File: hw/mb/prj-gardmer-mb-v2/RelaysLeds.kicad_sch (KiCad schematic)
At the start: 52 parts, among them K1 AZ9371T-1A-5D, K2 AZ9371T-1A-5D, K3 AZ9371T-1A-5D, K4 AZ9371T-1A-5D, Q1 BC817, Q13 BC817, Q14 BC817, Q2 BC817, Q3 BC817, Q4 BC817, U4 74HC595, U5 74HC595, U6 ULN2803A

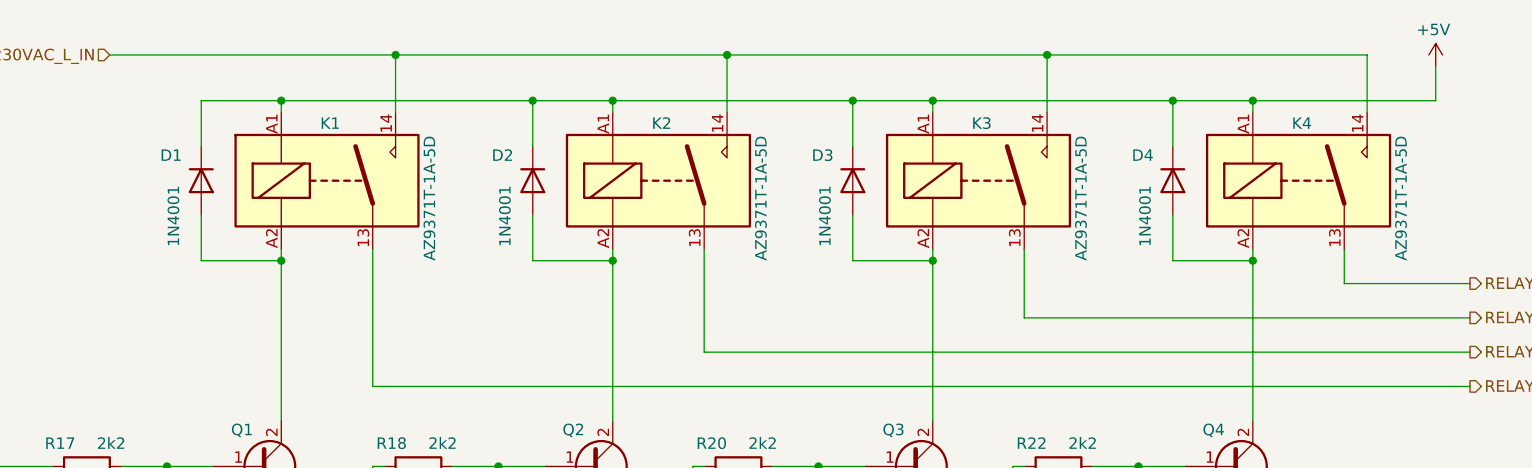
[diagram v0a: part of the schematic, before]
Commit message: Added footprints and bom. Updated schematics.
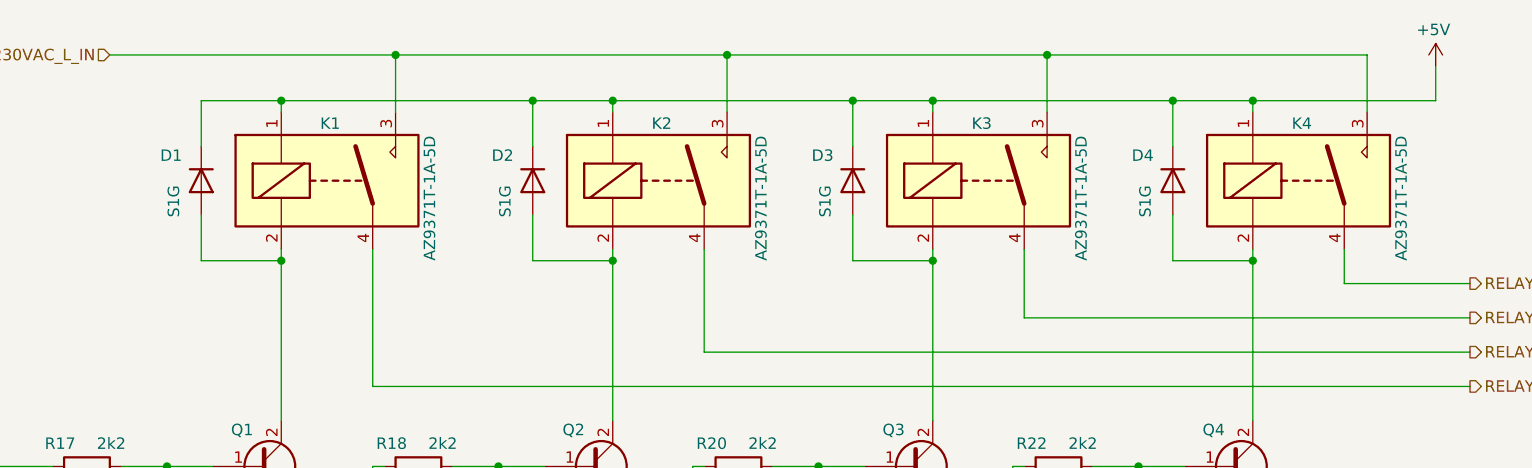
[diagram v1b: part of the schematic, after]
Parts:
- D1, D2, D3, D4: value 1N4001 -> S1G
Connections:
- net +5V: now also K1.1, K2.1, K3.1, K4.1; no longer K1.A1, K2.A1, K3.A1, K4.A1
- net 230VAC_L_IN: now also K1.3, K2.3, K3.3, K4.3; no longer K1.14, K2.14, K3.14, K4.14
- net RELAY1_OUT: now also K1.4; no longer K1.13
- net RELAY2_OUT: now also K2.4; no longer K2.13
- net RELAY3_OUT: now also K3.4; no longer K3.13
- net RELAY4_OUT: now also K4.4; no longer K4.13
- net at D4.2 (A), Q4.2 (C): now also K4.2; no longer K4.A2
- net at D1.2 (A), Q1.2 (C): now also K1.2; no longer K1.A2
- net at D2.2 (A), Q2.2 (C): now also K2.2; no longer K2.A2
- net at D3.2 (A), Q3.2 (C): now also K3.2; no longer K3.A2
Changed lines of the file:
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@@
 	)
 	(symbol
+		(lib_name "Relay_SPST-NO_1")
 		(lib_id "alf64:Relay_SPST-NO")
 		(at 138.43 31.75 0)
@@
 			)
 		)
-		(pin "13"
+		(pin "2"
 		)
-		(pin "A2"
+		(pin "1"
 		)
-		(pin "14"
+		(pin "3"
 		)
-		(pin "A1"
+		(pin "4"
 		)
 		(instances
@@
 			)
 		)
-		(property "Value" "1N4001"
+		(property "Value" "S1G"
 			(at 158.242 32.258 0)
 			(effects
@@
 			)
 		)
-		(property "Value" "1N4001"
+		(property "Value" "S1G"
 			(at 193.802 32.258 0)
 			(effects
@@
 	)
 	(symbol
+		(lib_name "Relay_SPST-NO_3")
 		(lib_id "alf64:Relay_SPST-NO")
 		(at 210.82 31.75 0)
@@
 			)
 		)
-		(pin "13"
+		(pin "1"
 		)
-		(pin "A2"
+		(pin "4"
 		)
-		(pin "14"
+		(pin "2"
 		)
-		(pin "A1"
+		(pin "3"
 		)
 		(instances
@@
 	)
 	(symbol
+		(lib_name "Relay_SPST-NO_2")
 		(lib_id "alf64:Relay_SPST-NO")
 		(at 175.26 31.75 0)
@@
 			)
 		)
-		(pin "13"
+		(pin "3"
 		)
-		(pin "A2"
+		(pin "1"
 		)
-		(pin "14"
+		(pin "2"
 		)
-		(pin "A1"
+		(pin "4"
 		)
 		(instances
@@
 			)
 		)
-		(property "Value" "1N4001"
+		(property "Value" "S1G"
 			(at 229.362 32.258 0)
 			(effects
@@
 			)
 		)
-		(pin "13"
+		(pin "1"
 		)
-		(pin "A2"
+		(pin "4"
 		)
-		(pin "14"
+		(pin "3"
 		)
-		(pin "A1"
+		(pin "2"
 		)
 		(instances
@@
 			)
 		)
-		(property "Value" "1N4001"
+		(property "Value" "S1G"
 			(at 121.412 32.258 0)
 			(effects

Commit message: Assigned footprints to schematic symbols.
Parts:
- C14, C15, C16, R16, R17, R18, R19, R20, R21, R22, R23, R24, R25, R26, R27, R28, R29, R30, R31, R48, R49, R50, R51, R52, R53: footprint (none) -> alf64:Generic_0805
- D1, D2, D3, D4: footprint (none) -> alf64:D_SMA
- D10, D11, D12, D13, D14, D5, D6, D7, D8, D9: footprint (none) -> alf64:D_0805
- K1, K2, K3, K4: footprint (none) -> alf64:relay_AZ9371
- Q1, Q13, Q14, Q2, Q3, Q4: footprint (none) -> alf64:SOT-23-3
- U4, U5: footprint (none) -> alf64:SO-16_3.9x9.9mm_P1.27mm
- U6: footprint (none) -> alf64:SOP-18_7x12.5mm_P1.27mm
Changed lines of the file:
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@@
 			)
 		)
-		(property "Footprint" ""
+		(property "Footprint" "alf64:SOT-23-3"
 			(at 243.84 60.96 0)
 			(effects
@@
 			)
 		)
-		(property "Footprint" ""
+		(property "Footprint" "alf64:Generic_0805"
 			(at 191.262 68.58 90)
 			(effects
@@
 			)
 		)
-		(property "Footprint" ""
+		(property "Footprint" "alf64:Generic_0805"
 			(at 53.0352 35.56 0)
 			(effects
@@
 			)
 		)
-		(property "Footprint" ""
+		(property "Footprint" "alf64:relay_AZ9371"
 			(at 149.86 33.02 0)
 			(effects
@@
 			)
 		)
-		(property "Footprint" ""
+		(property "Footprint" "alf64:D_SMA"
 			(at 161.29 31.75 0)
 			(effects
@@
 			)
 		)
-		(property "Footprint" ""
+		(property "Footprint" "alf64:D_0805"
 			(at 162.56 123.19 0)
 			(effects
@@
 			)
 		)
-		(property "Footprint" ""
+		(property "Footprint" "alf64:D_0805"
 			(at 162.56 110.49 0)
 			(effects
@@
 			)
 		)
-		(property "Footprint" ""
+		(property "Footprint" "alf64:D_0805"
 			(at 90.17 162.56 0)
 			(effects
@@
 			)
 		)
-		(property "Footprint" ""
+		(property "Footprint" "alf64:D_SMA"
 			(at 196.85 31.75 0)
 			(effects
@@
 			)
 		)
-		(property "Footprint" ""
+		(property "Footprint" "alf64:D_0805"
 			(at 162.56 152.4 0)
 			(effects
@@
 			)
 		)
-		(property "Footprint" ""
+		(property "Footprint" "alf64:SOT-23-3"
 			(at 92.71 170.18 0)
 			(effects
@@
 			)
 		)
-		(property "Footprint" ""
+		(property "Footprint" "alf64:Generic_0805"
 			(at 184.15 137.922 90)
 			(effects
@@
 			)
 		)
-		(property "Footprint" ""
+		(property "Footprint" "alf64:Generic_0805"
 			(at 118.872 68.58 90)
 			(effects
@@
 			)
 		)
-		(property "Footprint" ""
+		(property "Footprint" "alf64:relay_AZ9371"
 			(at 222.25 33.02 0)
 			(effects
@@
 			)
 		)
-		(property "Footprint" ""
+		(property "Footprint" "alf64:Generic_0805"
 			(at 155.702 68.58 90)
 			(effects
@@
 			)
 		)
-		(property "Footprint" ""
+		(property "Footprint" "alf64:SOP-18_7x12.5mm_P1.27mm"
 			(at 118.11 125.73 0)
 			(effects
@@
 			)
 		)
-		(property "Footprint" ""
+		(property "Footprint" "alf64:SOT-23-3"
 			(at 172.72 60.96 0)
 			(effects
@@
 			)
 		)
-		(property "Footprint" ""
+		(property "Footprint" "alf64:relay_AZ9371"
 			(at 186.69 33.02 0)
 			(effects
@@
 			)
 		)
-		(property "Footprint" ""
+		(property "Footprint" "alf64:Generic_0805"
 			(at 105.918 167.64 90)
 			(effects
@@
 			)
 		)
-		(property "Footprint" ""
+		(property "Footprint" "alf64:Generic_0805"
 			(at 65.7352 35.56 0)
 			(effects
@@
 			)
 		)
-		(property "Footprint" ""
+		(property "Footprint" "alf64:Generic_0805"
 			(at 148.59 65.278 90)
 			(effects
@@
 			)
 		)
-		(property "Footprint" ""
+		(property "Footprint" "alf64:D_SMA"
 			(at 232.41 31.75 0)
 			(effects
@@
 			)
 		)
-		(property "Footprint" ""
+		(property "Footprint" "alf64:Generic_0805"
 			(at 102.362 177.8 90)
 			(effects
@@
 			)
 		)
-		(property "Footprint" ""
+		(property "Footprint" "alf64:D_0805"
 			(at 162.56 116.84 0)
 			(effects
@@
 			)
 		)
-		(property "Footprint" ""
+		(property "Footprint" "alf64:Generic_0805"
 			(at 184.15 115.062 90)
 			(effects
@@
 			)
 		)
-		(property "Footprint" ""
+		(property "Footprint" "alf64:D_0805"
 			(at 162.56 139.7 0)
 			(effects
@@
 			)
 		)
-		(property "Footprint" ""
+		(property "Footprint" "alf64:Generic_0805"
 			(at 184.15 121.412 90)
 			(effects
@@
 			)
 		)
-		(property "Footprint" ""
+		(property "Footprint" "alf64:Generic_0805"
 			(at 40.3352 35.56 0)
 			(effects
@@
 			)
 		)
-		(property "Footprint" ""
+		(property "Footprint" "alf64:D_0805"
 			(at 162.56 146.05 0)
 			(effects
@@
 			)
 		)
-		(property "Footprint" ""
+		(property "Footprint" "alf64:Generic_0805"
 			(at 111.76 65.278 90)
 			(effects
@@
 			)
 		)
-		(property "Footprint" ""
+		(property "Footprint" "alf64:Generic_0805"
 			(at 184.15 65.278 90)
 			(effects
@@
 			)
 		)
-		(property "Footprint" ""
+		(property "Footprint" "alf64:D_0805"
 			(at 116.84 162.56 0)
 			(effects
@@
 			)
 		)
-		(property "Footprint" ""
+		(property "Footprint" "alf64:Generic_0805"
 			(at 115.062 153.67 90)
 			(effects
@@
 			)
 		)
-		(property "Footprint" ""
+		(property "Footprint" "alf64:Generic_0805"
 			(at 75.692 177.8 90)
 			(effects
@@
 			)
 		)
-		(property "Footprint" ""
+		(property "Footprint" "alf64:SO-16_3.9x9.9mm_P1.27mm"
 			(at 57.15 71.12 0)
 			(effects
@@
 			)
 		)
-		(property "Footprint" ""
+		(property "Footprint" "alf64:Generic_0805"
 			(at 79.248 167.64 90)
 			(effects
@@
 			)
 		)
-		(property "Footprint" ""
+		(property "Footprint" "alf64:Generic_0805"
 			(at 184.15 108.712 90)
 			(effects
@@
 			)
 		)
-		(property "Footprint" ""
+		(property "Footprint" "alf64:Generic_0805"
 			(at 219.71 65.278 90)
 			(effects
@@
 			)
 		)
-		(property "Footprint" ""
+		(property "Footprint" "alf64:D_0805"
 			(at 162.56 104.14 0)
 			(effects
@@
 			)
 		)
-		(property "Footprint" ""
+		(property "Footprint" "alf64:D_0805"
 			(at 162.56 133.35 0)
 			(effects
@@
 			)
 		)
-		(property "Footprint" ""
+		(property "Footprint" "alf64:Generic_0805"
 			(at 226.822 68.58 90)
 			(effects
@@
 			)
 		)
-		(property "Footprint" ""
+		(property "Footprint" "alf64:Generic_0805"
 			(at 88.392 153.67 90)
 			(effects
@@
 			)
 		)
-		(property "Footprint" ""
+		(property "Footprint" "alf64:Generic_0805"
 			(at 184.15 144.272 90)
 			(effects
@@
 			)
 		)
-		(property "Footprint" ""
+		(property "Footprint" "alf64:SOT-23-3"
 			(at 208.28 60.96 0)
 			(effects
@@
 			)
 		)
-		(property "Footprint" ""
+		(property "Footprint" "alf64:Generic_0805"
 			(at 184.15 102.362 90)
 			(effects
@@
 			)
 		)
-		(property "Footprint" ""
+		(property "Footprint" "alf64:relay_AZ9371"
 			(at 257.81 33.02 0)
 			(effects
@@
 			)
 		)
-		(property "Footprint" ""
+		(property "Footprint" "alf64:Generic_0805"
 			(at 184.15 150.622 90)
 			(effects
@@
 			)
 		)
-		(property "Footprint" ""
+		(property "Footprint" "alf64:SOT-23-3"
 			(at 135.89 60.96 0)
 			(effects
@@
 			)
 		)
-		(property "Footprint" ""
+		(property "Footprint" "alf64:D_SMA"
 			(at 124.46 31.75 0)
 			(effects
@@
 			)
 		)
-		(property "Footprint" ""
+		(property "Footprint" "alf64:SOT-23-3"
 			(at 119.38 170.18 0)
 			(effects
@@
 			)
 		)
-		(property "Footprint" ""
+		(property "Footprint" "alf64:SO-16_3.9x9.9mm_P1.27mm"
 			(at 57.15 121.92 0)
 			(effects
@@
 			)
 		)
-		(property "Footprint" ""
+		(property "Footprint" "alf64:Generic_0805"
 			(at 184.15 131.572 90)
 			(effects

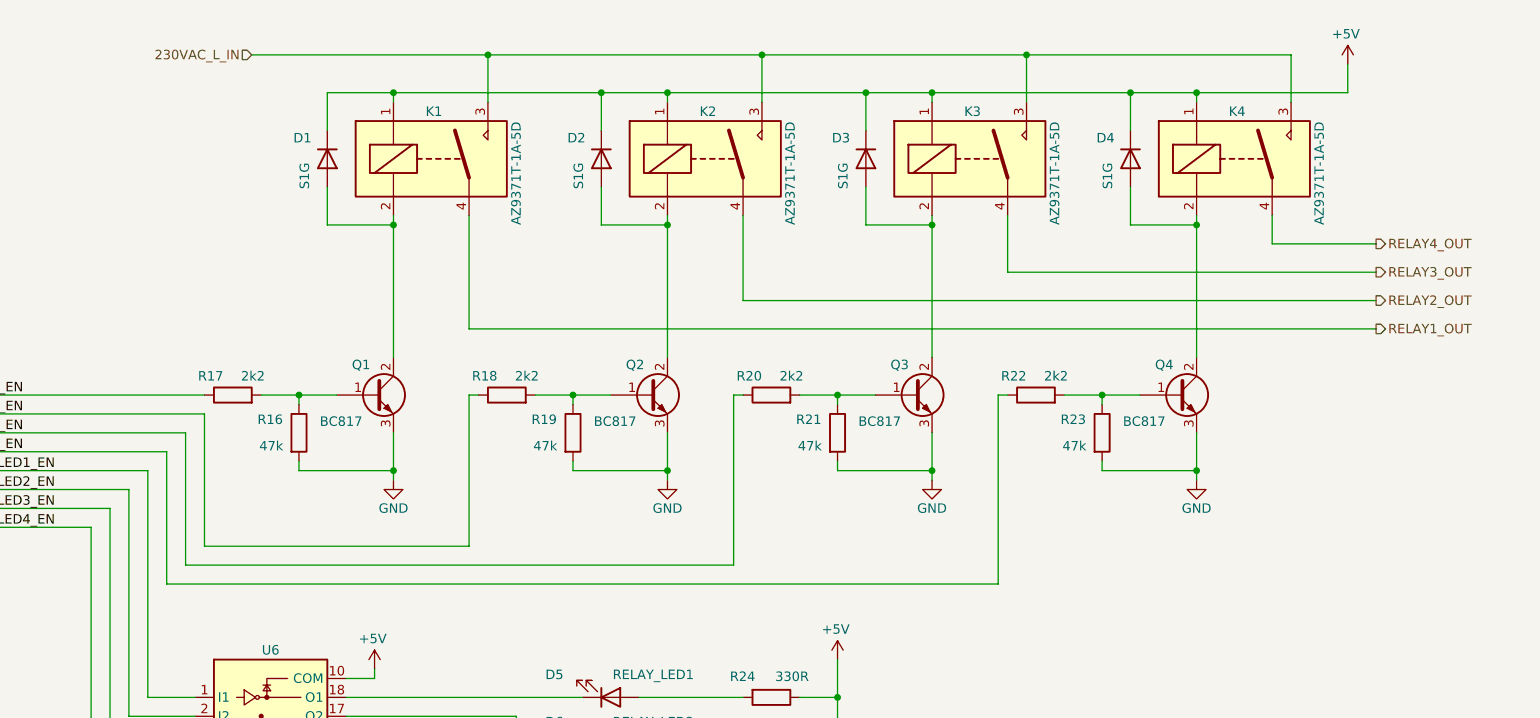
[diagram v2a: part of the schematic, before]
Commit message: Updated schematic: - added test points instead of connections between relays and outputs - fixed crystal connection for rtc
Updated PCB:
- halfway through the routing

Updated footprints:
- added footprints for test points
- reduced size of pads for D_SMA
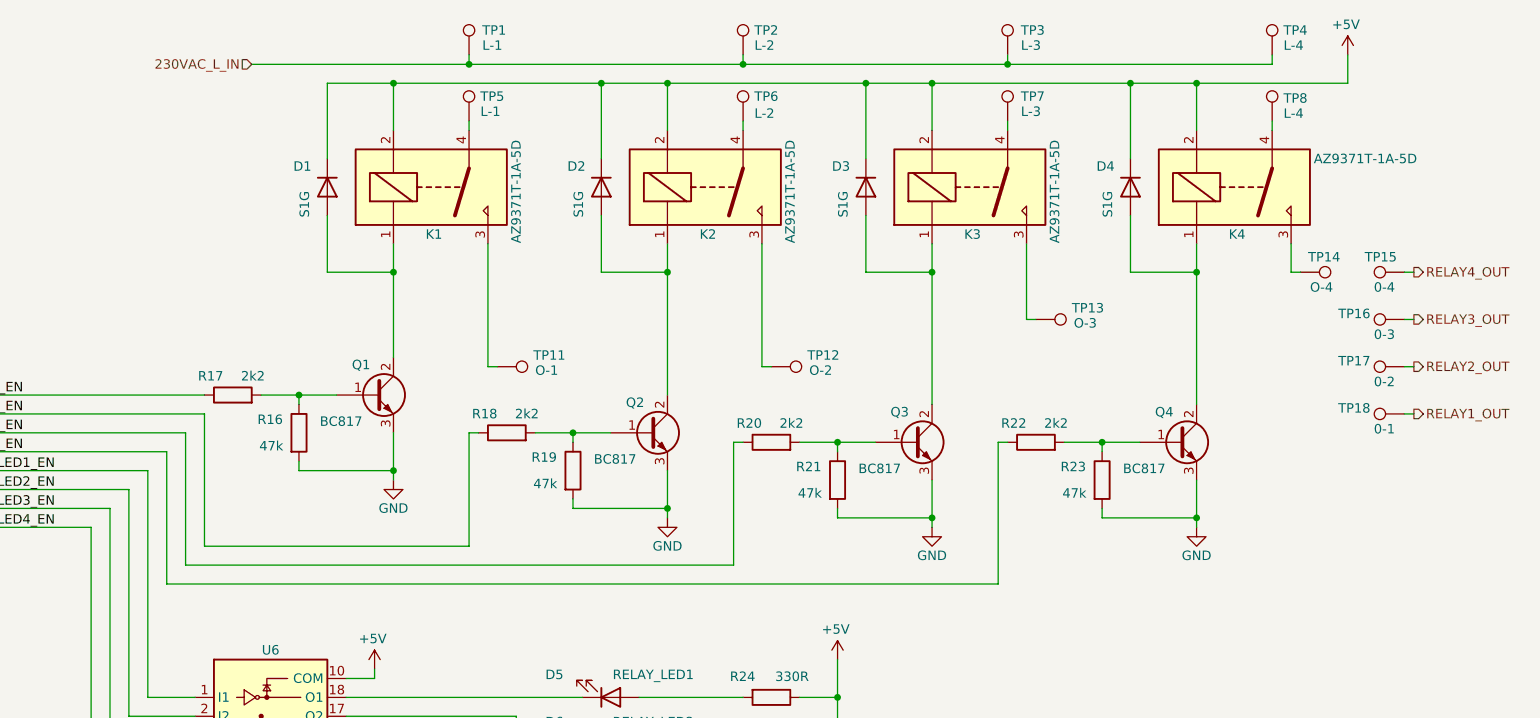
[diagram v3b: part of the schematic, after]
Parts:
- added TP1, TP5: L-1, alf64:TestPoint_Pad_2.5x2.5mm_NoBorders, symbol alf64:TestPoint
- added TP11: O-1, alf64:TestPoint_Pad_2.5x2.5mm_NoBorders, symbol alf64:TestPoint
- added TP12: O-2, alf64:TestPoint_Pad_2.5x2.5mm_NoBorders, symbol alf64:TestPoint
- added TP13: O-3, alf64:TestPoint_Pad_2.5x2.5mm_NoBorders, symbol alf64:TestPoint
- added TP14: O-4, alf64:TestPoint_Pad_2.5x2.5mm_NoBorders, symbol alf64:TestPoint
- added TP15: 0-4, alf64:TestPoint_Pad_2.5x2.5mm_NoBorders, symbol alf64:TestPoint
- added TP16: 0-3, alf64:TestPoint_Pad_2.5x2.5mm_NoBorders, symbol alf64:TestPoint
- added TP17: 0-2, alf64:TestPoint_Pad_2.5x2.5mm_NoBorders, symbol alf64:TestPoint
- added TP18: 0-1, alf64:TestPoint_Pad_2.5x2.5mm_NoBorders, symbol alf64:TestPoint
- added TP2, TP6: L-2, alf64:TestPoint_Pad_2.5x2.5mm_NoBorders, symbol alf64:TestPoint
- added TP3, TP7: L-3, alf64:TestPoint_Pad_2.5x2.5mm_NoBorders, symbol alf64:TestPoint
- added TP4, TP8: L-4, alf64:TestPoint_Pad_2.5x2.5mm_NoBorders, symbol alf64:TestPoint
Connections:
- net +5V: now also K1.2, K2.2, K3.2, K4.2; no longer K1.1, K2.1, K3.1, K4.1
- net 230VAC_L_IN: now also TP1.1, TP2.1, TP3.1, TP4.1; no longer K1.3, K2.3, K3.3, K4.3
- net RELAY1_OUT: now also TP18.1; no longer K1.4
- net RELAY2_OUT: now also TP17.1; no longer K2.4
- net RELAY3_OUT: now also TP16.1; no longer K3.4
- net RELAY4_OUT: now also TP15.1; no longer K4.4
- net at D4.2 (A), Q4.2 (C): now also K4.1; no longer K4.2
- net at D1.2 (A), Q1.2 (C): now also K1.1; no longer K1.2
- net at D2.2 (A), Q2.2 (C): now also K2.1; no longer K2.2
- net at D3.2 (A), Q3.2 (C): now also K3.1; no longer K3.2
- new net: K1.3, TP11.1
- new net: K1.4, TP5.1
- new net: K2.4, TP6.1
- new net: K4.3, TP14.1
- new net: K3.3, TP13.1
- new net: K3.4, TP7.1
- new net: K2.3, TP12.1
- new net: K4.4, TP8.1
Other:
- moved on the sheet: D1, D2, D3, D4, K1, K2, K3, K4, Q2, Q3, Q4, R18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
